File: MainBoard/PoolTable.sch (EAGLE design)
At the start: 80 parts, among them IC1 LM317MBSTT3, IC2 LM317MBSTT3, IC3 LM317MBSTT3, IC4 ESD5384NCTBG, IC5 MIC2026-1YM, IC7 AP2331W-7, J1 USB_A_SMT_FEMALE, J2 USB_A_SMT_FEMALE, J4 SD_CARD_SOCKET, Q1 DMG1012T-7, Q2 DMG1012T-7, Q3 DMG1012T-7, Q4 DMG1012T-7, U1 TMP102, U2 TMP102, U3 TMP102, U4 TMP102, U5 LAN9512-JZX, U6 FSUSB42UMX

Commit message: Finished HDMI
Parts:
- added Q5: DMG1012T-7, SamacSys_Parts:DMG1012T-7
- added R26: 100K, SparkFun-Resistors:100KOHM-0402-1/16W-1%
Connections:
- new net HDMI_CEC: CPU1.171/HDMI_CEC
- new net HDMI_CK_N: CPU1.111/HDMI_CK_N*
- new net HDMI_CK_P: CPU1.113/HDMI_CK_P*
- new net HDMI_D0_N: CPU1.117/HDMI_D0_N*
- new net HDMI_D0_P: CPU1.119/HDMI_D0_P*
- new net HDMI_D1_N: CPU1.123/HDMI_D1_N*
- new net HDMI_D1_P: CPU1.125/HDMI_D1_P*
- new net HDMI_D2_N: CPU1.129/HDMI_D2_N*
- new net HDMI_D2_P: CPU1.131/HDMI_D2_P*
- new net HDMI_HPD_N_1V8: CPU1.88/GPIO46_1V8
- new net HDMI_SCL: CPU1.175/HDMI_SCL
- new net HDMI_SDA: CPU1.173/HDMI_SDA
- new net N$13: Q4.S
- new net N$14: Q5.D, R26.2
- new net N$24: U$6.UTIL
- new net N$25: U$6.CLOCK-
- new net N$26: U$6.CLOCK+
- new net N$27: U$6.DATA0-
- new net N$28: U$6.DATA0+
- new net N$29: U$6.DATA1-
- new net N$30: U$6.DATA1+
- new net N$31: U$6.DATA2-
- new net N$32: U$6.DATA2+
- new net N$33: IC4.RPU2
- net 1.8V: now also R26.1
- net GND: now also Q5.S
- net N$7: now also Q4.D; no longer Q4.S
- net N$8: now also Q5.G
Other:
- moved on the sheet: Q4

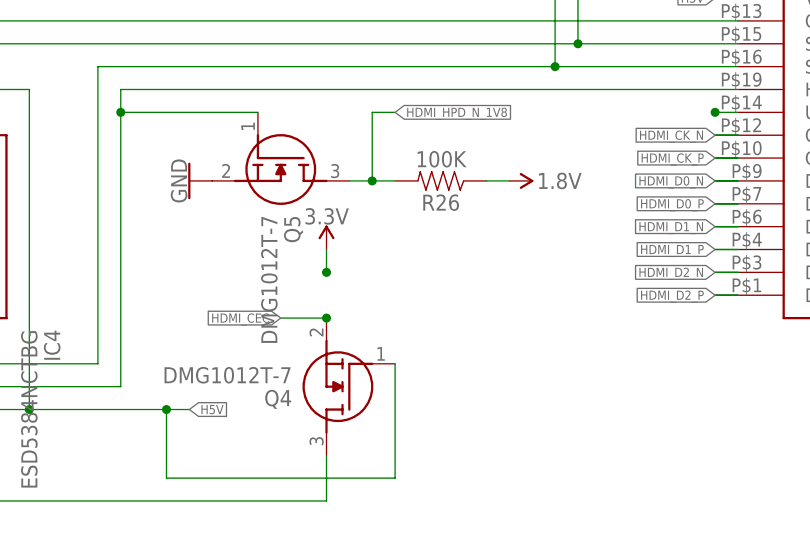
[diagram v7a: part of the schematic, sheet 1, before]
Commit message: Added solder jumper for HDMI
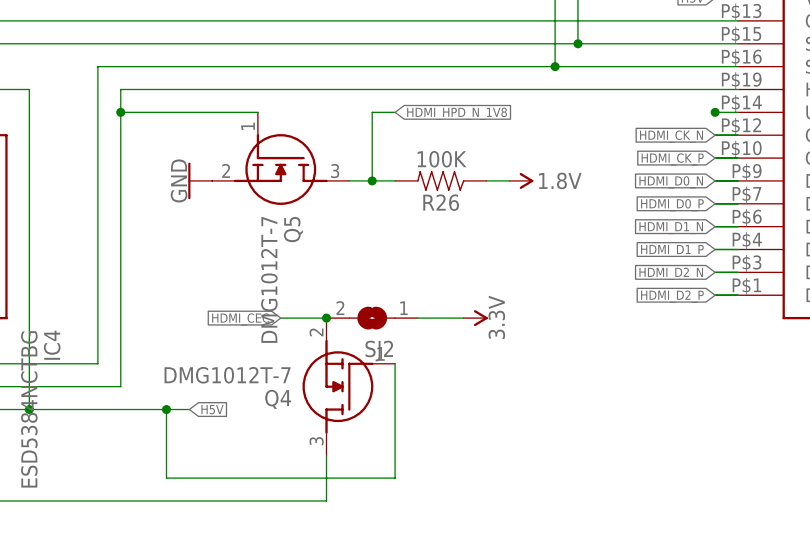
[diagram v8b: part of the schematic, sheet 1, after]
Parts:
- added SJ2: (no value), jumper:SJ
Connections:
- net 3.3V: now also SJ2.1
- net N$13: now also SJ2.2
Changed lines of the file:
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@@
 <part name="R26" library="SparkFun-Resistors" library_urn="urn:adsk.eagle:library:532" deviceset="100KOHM" device="-0402-1/16W-1%" package3d_urn="urn:adsk.eagle:package:39657/1" value="100K"/>
 <part name="SUPPLY54" library="SparkFun-PowerSymbols" deviceset="1.8V" device=""/>
+<part name="SJ2" library="jumper" library_urn="urn:adsk.eagle:library:252" deviceset="SJ" device="" package3d_urn="urn:adsk.eagle:package:15471/1"/>
 </parts>
 <sheets>
@@
 <attribute name="VALUE" x="281.94" y="724.154" size="1.778" layer="96" align="bottom-center"/>
 </instance>
-<instance part="SUPPLY53" gate="G$1" x="330.2" y="33.02" smashed="yes">
-<attribute name="VALUE" x="330.2" y="35.814" size="1.778" layer="96" align="bottom-center"/>
+<instance part="SUPPLY53" gate="G$1" x="345.44" y="25.4" smashed="yes" rot="R270">
+<attribute name="VALUE" x="348.234" y="25.4" size="1.778" layer="96" rot="R270" align="bottom-center"/>
 </instance>
 <instance part="Q5" gate="G$1" x="322.58" y="48.26" smashed="yes" rot="R270">
@@
 <instance part="SUPPLY54" gate="G$1" x="350.52" y="40.64" smashed="yes" rot="R270">
 <attribute name="VALUE" x="353.568" y="40.64" size="1.778" layer="96" align="center-left"/>
+</instance>
+<instance part="SJ2" gate="1" x="335.28" y="25.4" smashed="yes" rot="R180">
+<attribute name="NAME" x="337.82" y="22.86" size="1.778" layer="95" rot="R180"/>
+<attribute name="VALUE" x="337.82" y="29.21" size="1.778" layer="96" rot="R180"/>
 </instance>
 </instances>
@@
 </segment>
 <segment>
-<wire x1="330.2" y1="30.48" x2="330.2" y2="33.02" width="0.1524" layer="91"/>
+<pinref part="SJ2" gate="1" pin="1"/>
 <pinref part="SUPPLY53" gate="G$1" pin="3.3V"/>
-<junction x="330.2" y="30.48"/>
+<wire x1="340.36" y1="25.4" x2="345.44" y2="25.4" width="0.1524" layer="91"/>
 </segment>
 </net>
@@
 <wire x1="325.12" y1="25.4" x2="330.2" y2="25.4" width="0.1524" layer="91"/>
 <junction x="330.2" y="25.4"/>
-</segment>
-</net>
+<pinref part="SJ2" gate="1" pin="2"/>
+</segment>
+</net>
